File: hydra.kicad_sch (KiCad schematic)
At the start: 23 parts, among them J1 Micro_SD_Card, J2 PC104 Interconnect, U1 AMS1117-3.3

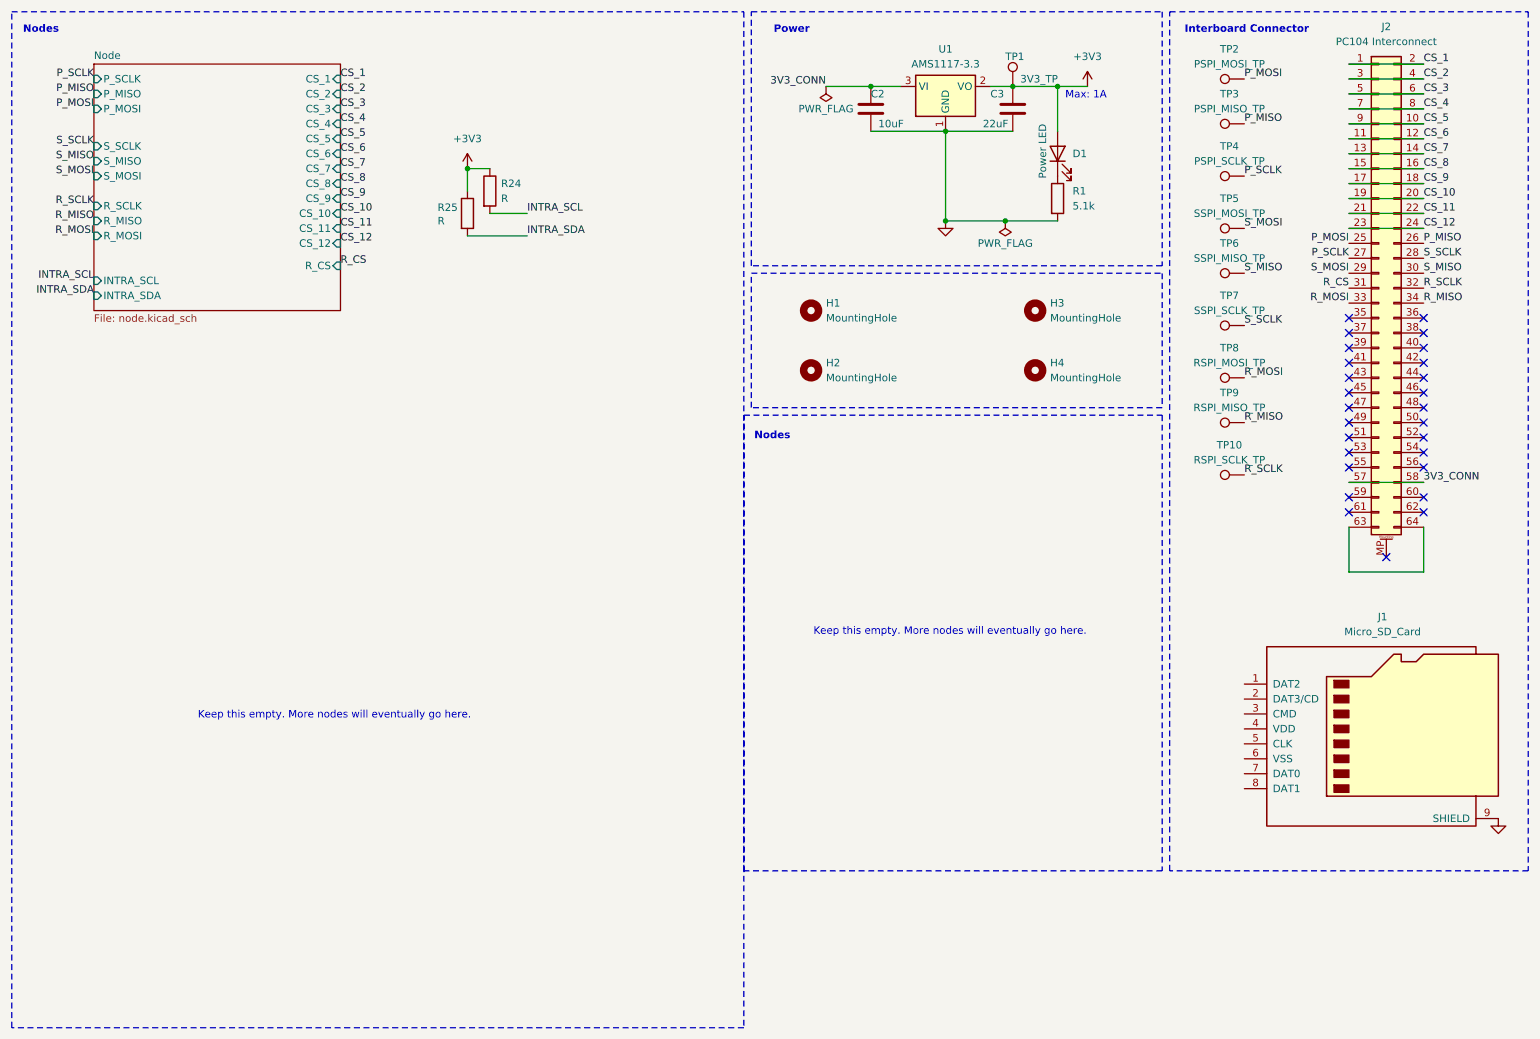
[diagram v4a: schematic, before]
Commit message: switch to STM32L431
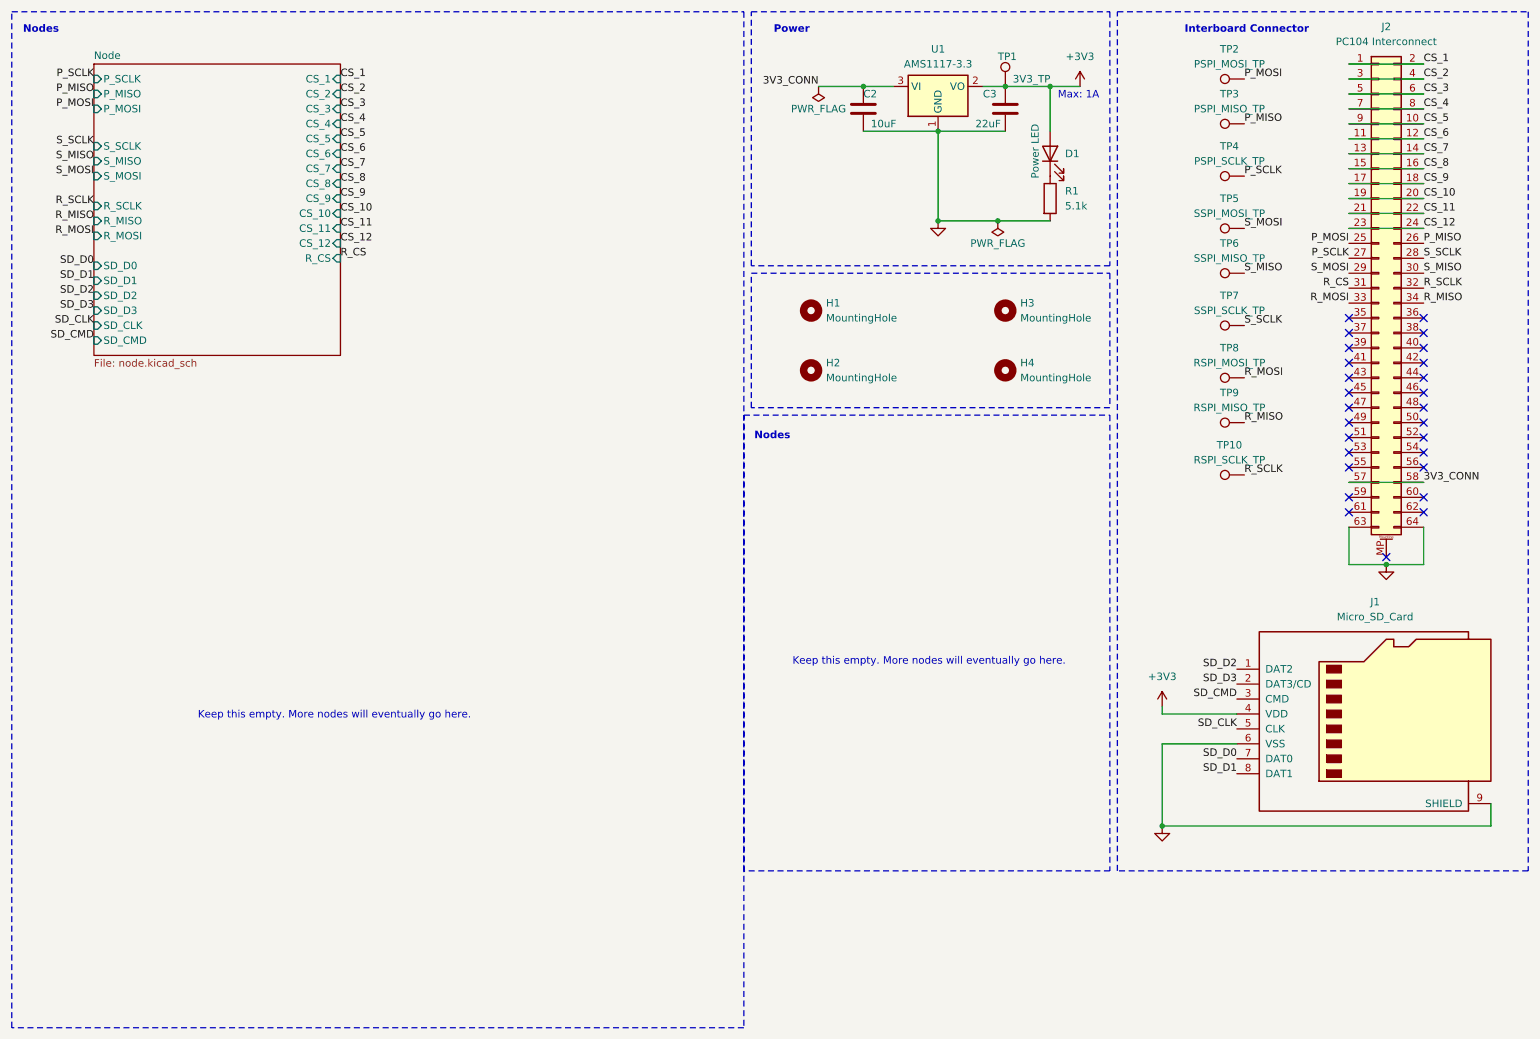
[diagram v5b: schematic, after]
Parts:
- removed R24, R25: R, symbol Device:R
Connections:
- net +3V3: now also J1.4 (VDD)
- net GND: now also J1.6 (VSS), J2.63 (Pin_63), J2.64 (Pin_64)
- net SD_D2: now reaches J1.1 (DAT2)
- net SD_D3: now reaches J1.2 (DAT3/CD)
- net SD_CMD: now reaches J1.3 (CMD)
- net SD_CLK: now reaches J1.5 (CLK)
- net SD_D0: now reaches J1.7 (DAT0)
- net SD_D1: now reaches J1.8 (DAT1)
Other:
- sheet Node ports: added SD_CLK, SD_CMD, SD_D0, SD_D1, SD_D2, SD_D3; removed INTRA_SCL, INTRA_SDA
- moved on the sheet: C2, C3, D1, H3, H4, R1, TP1, U1
